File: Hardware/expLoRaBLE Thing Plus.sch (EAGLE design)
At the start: 67 parts, among them J2 CORTEX_DEBUG, J5 USB-C, J8 U.FL, U1 MCP73831, U2 3.3V, U3 NM180100, U4 CH340E_MSOP10, U6 DPX202700DT-4162A1, Y1 32.768kHz

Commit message: Made changes per review meeting, added FCC ID
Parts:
- added TP6: TEST-POINTTP_15TH_THRU, SparkFun-Connectors:TEST-POINTTP_15TH_THRU
- ISO: value JUMPER-SMT_2_NC_TRACE_NO-SILK -> JUMPER-SMT_2_NC_TRACE_SILK; device SparkFun-Jumpers:JUMPER-SMT_2_NC_TRACE_NO-SILK -> SparkFun-Jumpers:JUMPER-SMT_2_NC_TRACE_SILK
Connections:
- net SWDCK: now also TP6.1

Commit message: Added NO jumper for RTS - RESET
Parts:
- added C1: 0.1uF, SparkFun-Capacitors:0.1UF-0603-25V-(+80/-20%)
- added JP1: JUMPER-SMT_2_NO_SILK, SparkFun-Jumpers:JUMPER-SMT_2_NO_SILK
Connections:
- new net !RTS: C1.1, U4.!RTS
- new net N$15: C1.2, JP1.1
- net !RESET: now also JP1.2
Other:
- moved on the sheet: C15, R11, S1

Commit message: RTS jumper buzzard label
-renamed jumper to "RTS"
-added buzzard label
-also moved user silk "10" to new button position
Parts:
- renumbered JP1 to RTS
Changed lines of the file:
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@@
 <part name="TP6" library="SparkFun-Connectors" library_urn="urn:adsk.eagle:library:513" deviceset="TEST-POINT" device="TP_15TH_THRU" package3d_urn="urn:adsk.eagle:package:38288/1"/>
 <part name="C1" library="SparkFun-Capacitors" library_urn="urn:adsk.eagle:library:510" deviceset="0.1UF" device="-0603-25V-(+80/-20%)" package3d_urn="urn:adsk.eagle:package:37414/1" value="0.1uF"/>
-<part name="JP1" library="SparkFun-Jumpers" library_urn="urn:adsk.eagle:library:528" deviceset="JUMPER-SMT_2_NO" device="_SILK" package3d_urn="urn:adsk.eagle:package:39279/1"/>
+<part name="RTS" library="SparkFun-Jumpers" library_urn="urn:adsk.eagle:library:528" deviceset="JUMPER-SMT_2_NO" device="_SILK" package3d_urn="urn:adsk.eagle:package:39279/1"/>
 </parts>
 <sheets>
@@
 <attribute name="VALUE" x="14.859" y="44.704" size="1.778" layer="96" font="vector" rot="R90"/>
 </instance>
-<instance part="JP1" gate="G$1" x="27.94" y="53.34" smashed="yes">
-<attribute name="NAME" x="25.4" y="55.88" size="1.778" layer="95" font="vector"/>
+<instance part="RTS" gate="G$1" x="27.94" y="53.34" smashed="yes">
+<attribute name="NAME" x="26.162" y="55.372" size="1.778" layer="95" font="vector"/>
 </instance>
 </instances>
@@
 <junction x="38.1" y="53.34"/>
 <wire x1="38.1" y1="53.34" x2="35.56" y2="53.34" width="0.1524" layer="91"/>
-<pinref part="JP1" gate="G$1" pin="2"/>
+<pinref part="RTS" gate="G$1" pin="2"/>
 <wire x1="35.56" y1="53.34" x2="34.1884" y2="53.34" width="0.1524" layer="91"/>
 <wire x1="33.02" y1="53.34" x2="34.1884" y2="53.34" width="0.1524" layer="91"/>
@@
 <segment>
 <pinref part="C1" gate="G$1" pin="2"/>
-<pinref part="JP1" gate="G$1" pin="1"/>
+<pinref part="RTS" gate="G$1" pin="1"/>
 <wire x1="20.32" y1="53.34" x2="22.86" y2="53.34" width="0.1524" layer="91"/>
 </segment>

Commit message: checklist run
-added text blurb explaining optional RTS jumper
-approved one gnd wire stub off of ch340
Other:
- note added: "RTS Jumper is optional. Closing this allows the user reset the module from the CH340E IC via software."
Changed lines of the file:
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@@
 <wire x1="68.58" y1="96.52" x2="68.58" y2="0" width="0.2032" layer="97" style="longdash"/>
 <text x="238.76" y="7.62" size="2.54" layer="94" font="vector">v01</text>
+<text x="10.16" y="17.78" size="1.778" layer="97" font="vector">RTS Jumper is optional.
+Closing this allows the user
+reset the module from the
+CH340E IC via software.</text>
+<wire x1="27.94" y1="50.8" x2="17.78" y2="30.48" width="0.2032" layer="97" style="shortdash"/>
 </plain>
 <instances>

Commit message: Fixed short from 3.3V to GND caused by USB connector mill holes
Adjusted inner layer polygons to not pour under the USB connector. Previously these were shorting all planes together, causing a short between 3.3V NET and GND NET.
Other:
- note added: "v02"
- note removed: "v01"
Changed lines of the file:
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@@
 <text x="193.04" y="174.498" size="1.778" layer="97" font="vector">VIN: 6V Max</text>
 <text x="168.656" y="11.43" size="2.54" layer="94" font="vector">Daniel Dobre</text>
-<text x="238.76" y="7.62" size="2.54" layer="94" font="vector">v01</text>
+<text x="238.76" y="7.62" size="2.54" layer="94" font="vector">v02</text>
 <text x="222.25" y="179.07" size="1.778" layer="97" font="vector">Cut LED jumper
 to disable power LED</text>
@@
 <text x="168.656" y="11.43" size="2.54" layer="94" font="vector">Daniel Dobre</text>
 <wire x1="68.58" y1="96.52" x2="68.58" y2="0" width="0.2032" layer="97" style="longdash"/>
-<text x="238.76" y="7.62" size="2.54" layer="94" font="vector">v01</text>
+<text x="238.76" y="7.62" size="2.54" layer="94" font="vector">v02</text>
 <text x="10.16" y="17.78" size="1.778" layer="97" font="vector">RTS Jumper is optional.
 Closing this allows the user

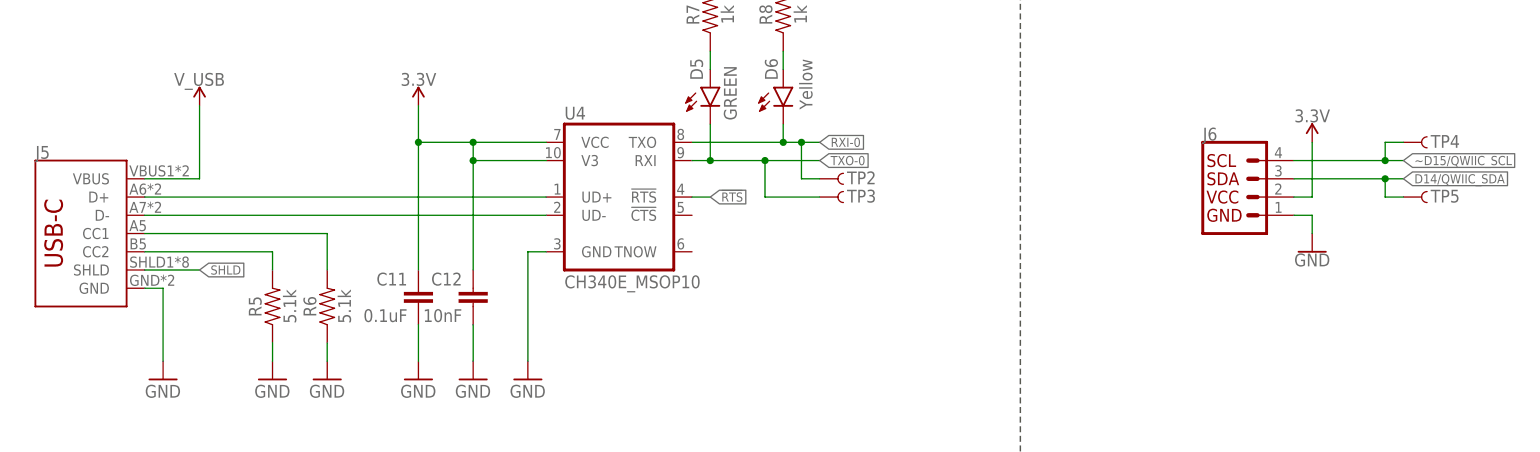
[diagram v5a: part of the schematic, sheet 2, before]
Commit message: Updating to USB-C-16P-4-LAYER-ISOLATED
-This new footprint includes the isolation (aka cutout polygons). It is better to include these at the library lavel (rather than in the board, as it was previously).

-Note, had to re-route VBUS, because the update also included moving the pads south to match the datasheet. This update commit history to the connector library here: https://github.com/sparkfun/SparkFun-Eagle-Libraries/commit/385c00bb90b92dfd747075cffe71177065b70510#diff-c73d36e753812bf738f1d00b48f2ac4ee18b59eb919db6021d587bb22fbbb9cd
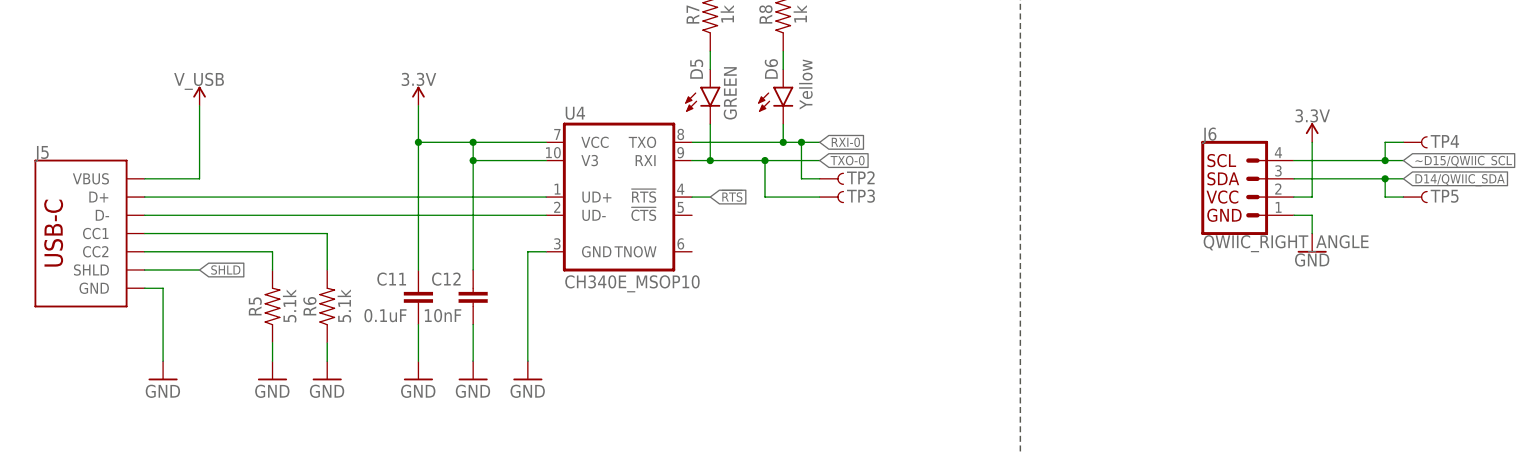
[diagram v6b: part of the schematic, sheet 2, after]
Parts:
- J5: value USB-C -> USB Female Type C Connector; device SparkFun-Connectors:USB_C2-LAYER -> SparkFun-Connectors:USB_C_4-LAYER-ISOLATED
- J6: value (none) -> QWIIC_RIGHT_ANGLE
